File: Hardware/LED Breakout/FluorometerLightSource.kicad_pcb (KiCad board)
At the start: 2 copper layers, 50.8 x 57.1 mm, 31 parts, among them Q1 BSS214NW, Q2 BSS214NW, Q3 BSS214NW, Q4 BSS214NW, Q5 BSS214NW, Q6 BSS214NW, Q7 BSS214NW, Q8 BSS214NW

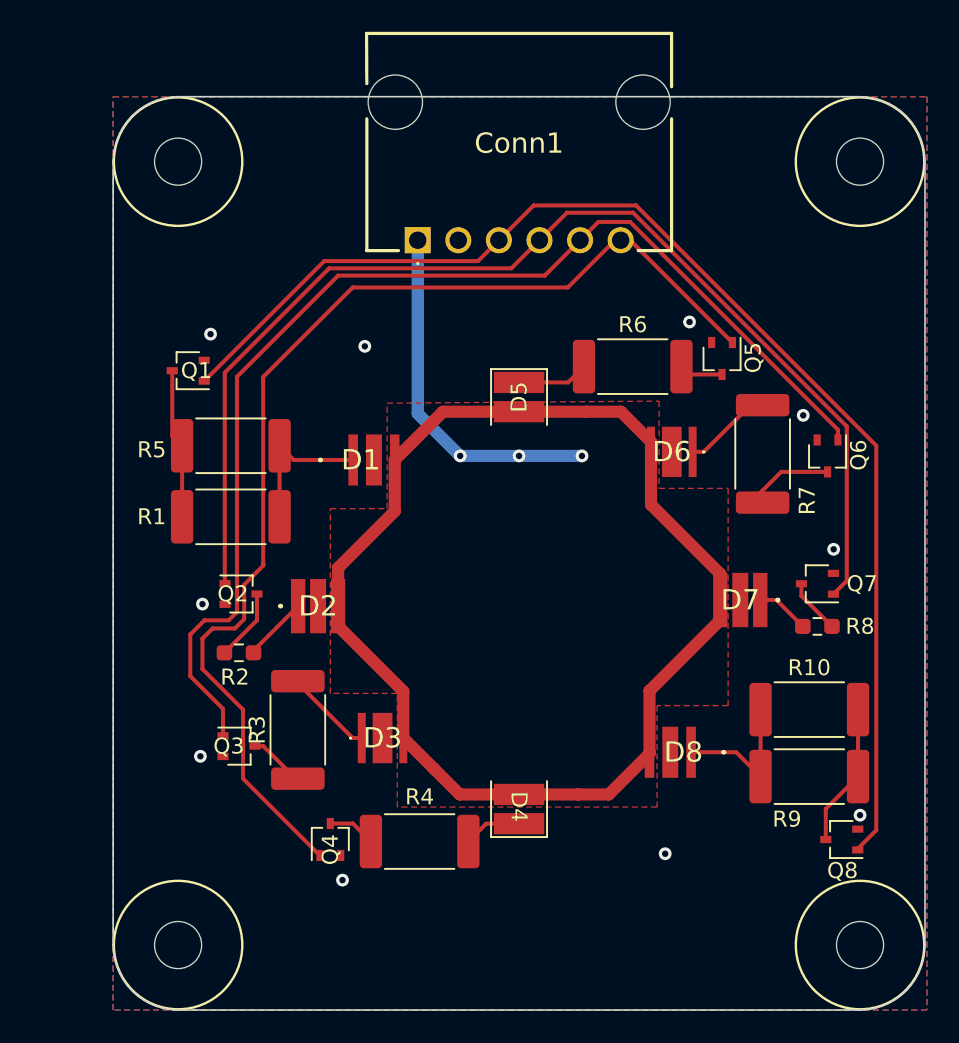
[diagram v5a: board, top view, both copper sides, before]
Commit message: Added indicators to LED breakout + made gerbs
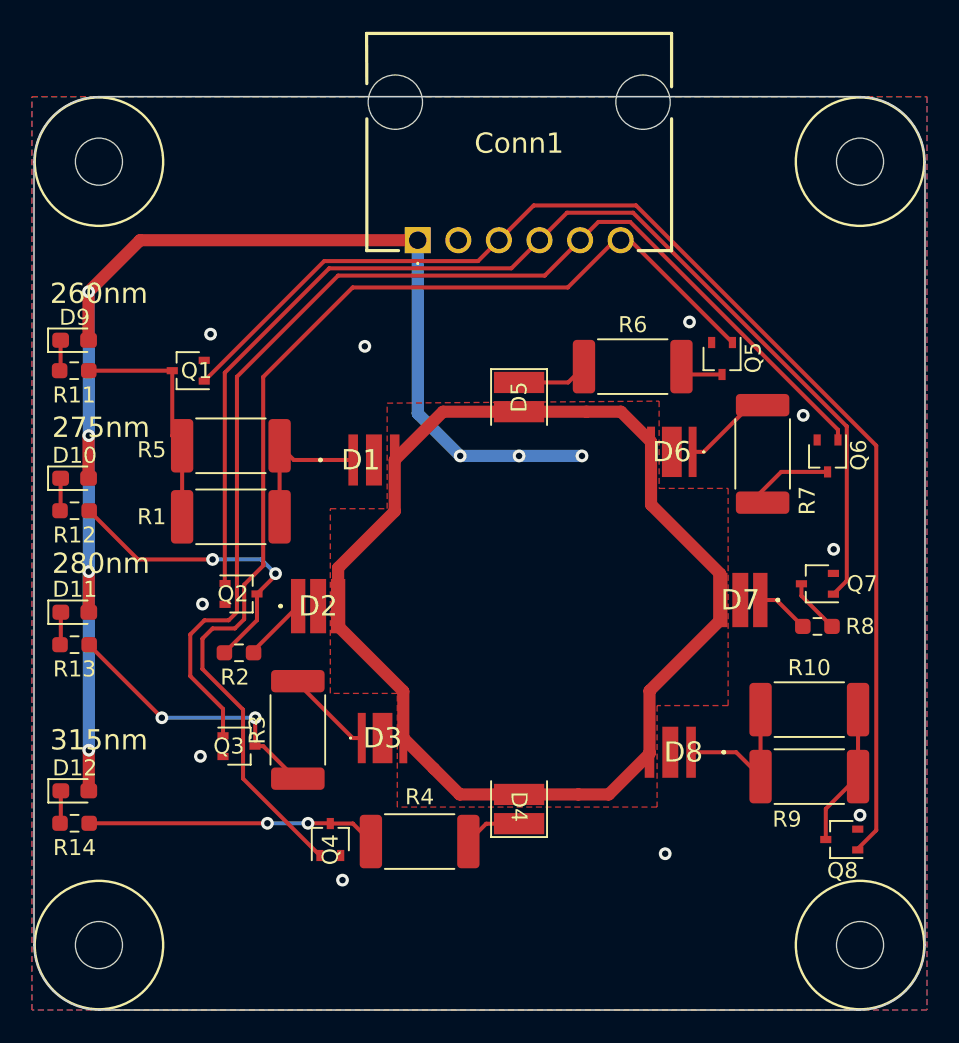
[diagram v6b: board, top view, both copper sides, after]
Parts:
- added D10: Green, LED_SMD:LED_0603_1608Metric_Pad1.05x0.95mm_HandSolder, F.Cu at (134.6, 102.4)
- added D11: Green, LED_SMD:LED_0603_1608Metric_Pad1.05x0.95mm_HandSolder, F.Cu at (134.6, 110.7)
- added D12: Green, LED_SMD:LED_0603_1608Metric_Pad1.05x0.95mm_HandSolder, F.Cu at (134.6, 121.9)
- added D9: Green, LED_SMD:LED_0603_1608Metric_Pad1.05x0.95mm_HandSolder, F.Cu at (134.6, 93.7)
- added R11: 120, Resistor_SMD:R_0603_1608Metric_Pad0.98x0.95mm_HandSolder, F.Cu at (134.6, 95.6)
- added R12: 120, Resistor_SMD:R_0603_1608Metric_Pad0.98x0.95mm_HandSolder, F.Cu at (134.6, 104.4)
- added R13: 120, Resistor_SMD:R_0603_1608Metric_Pad0.98x0.95mm_HandSolder, F.Cu at (134.6, 112.8)
- added R14: 120, Resistor_SMD:R_0603_1608Metric_Pad0.98x0.95mm_HandSolder, F.Cu at (134.6, 124.0)
- moved V3 4.95 mm to (136.1, 82.5)
- moved V4 4.95 mm to (136.1, 131.6)
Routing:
- net +12V: track 101.9 -> 163.3 mm, vias 3 -> 7
- net Net-(R4-Pad2): track 3.00 -> 18.1 mm, vias 0 -> 2
- net Net-(R2-Pad2): track 4.53 -> 19.6 mm, vias 0 -> 2
- net Net-(R3-Pad2): track 3.53 -> 17.6 mm, vias 0 -> 2
- net Net-(R1-Pad2): track 9.40 -> 14.6 mm
- net Net-(D11-Pad1): track 0.00 -> 2.05 mm
- net Net-(D12-Pad1): track 0.00 -> 2.05 mm
- net Net-(D10-Pad1): track 0.00 -> 2.05 mm
- net Net-(D9-Pad1): track 0.00 -> 1.93 mm
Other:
- board size 50.8 x 57.1 mm -> 55.8 x 57.1 mm
- board text added: "260nm"
- board text added: "275nm"
- board text added: "280nm"
- board text added: "315nm"
